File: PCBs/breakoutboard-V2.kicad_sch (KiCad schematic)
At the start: 38 parts, among them IC1 PASCO2V01BUMA1, J1 Conn_01x12_FPC_0.5mm, J2 Qwiic_RA, J4 SM06B-GHS-TB, J5 USB_C_Receptacle, SW1 SMD_4.6x2.8mm_h2.5mm, SW2 SMD_4.6x2.8mm_h2.5mm, SW3 PTH_RA_h7.5mm, U1 AP3012, U2 ESP32-S3-WROOM-1-N16R2, U5 AP2112K-3.3

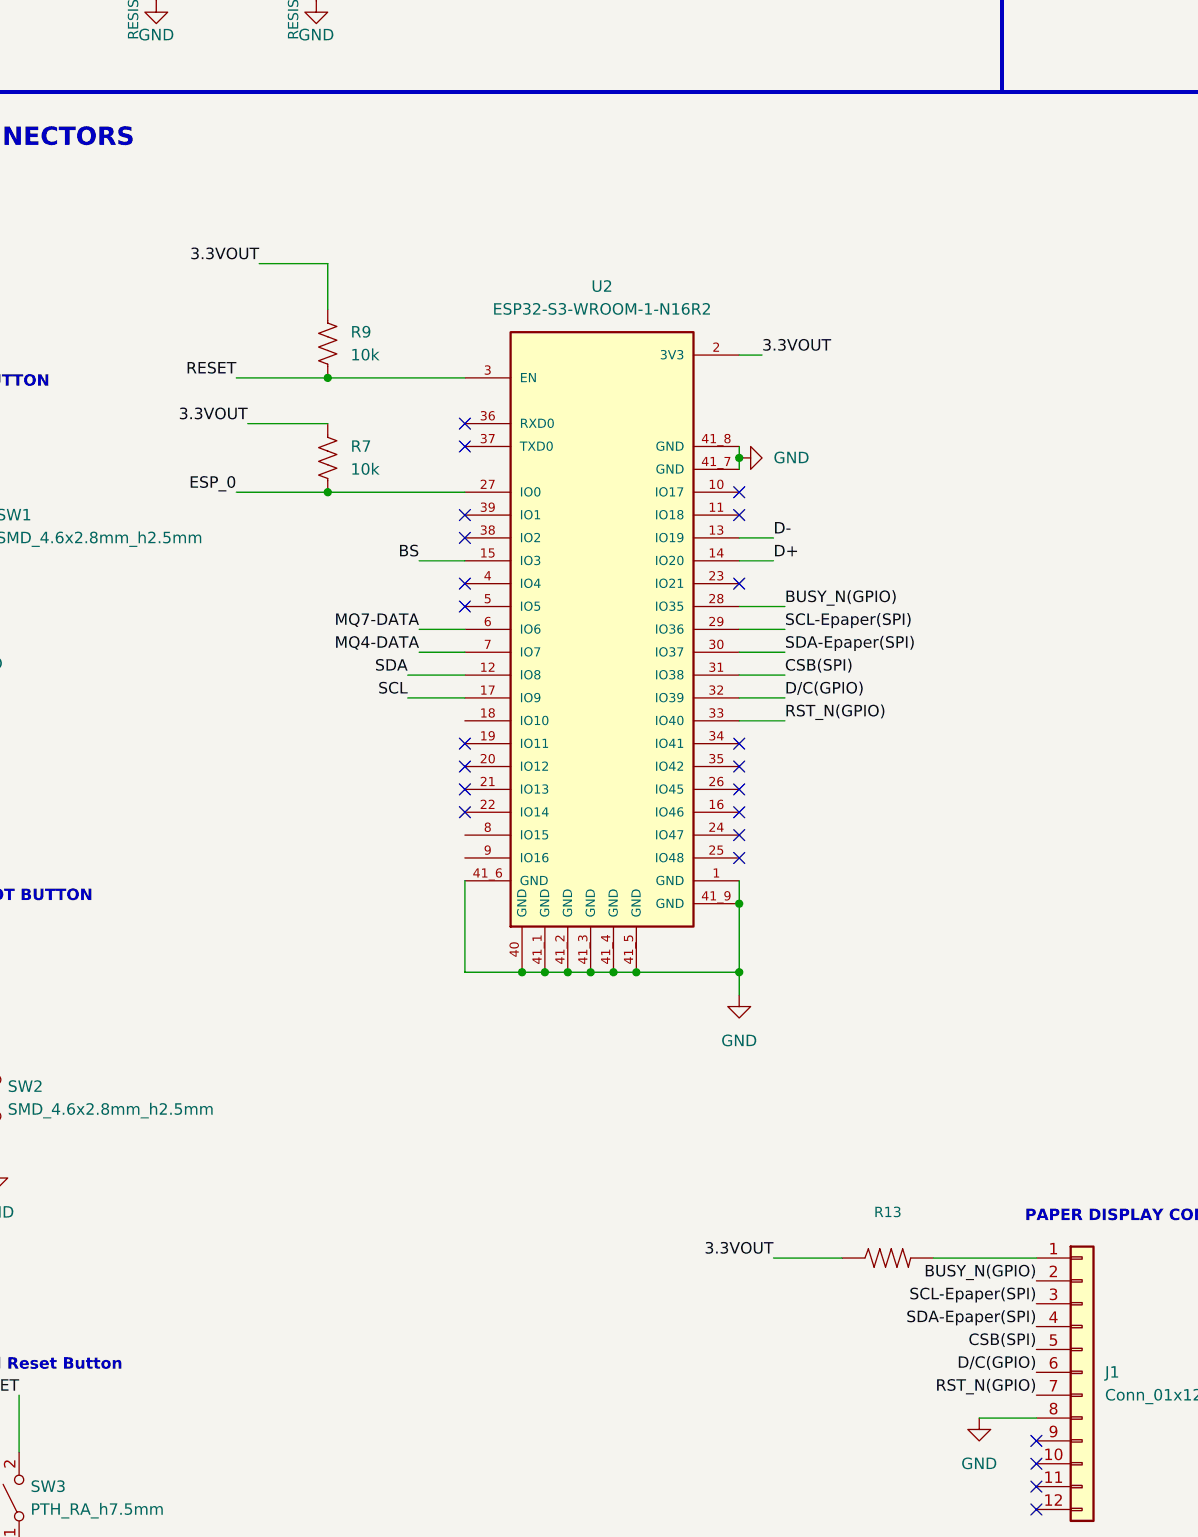
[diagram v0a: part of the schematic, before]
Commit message: Update Main Board PCB
Replaced ESP32 WROOM with ESP32 mini. READY FOR AIR WIRE REVIEW :D
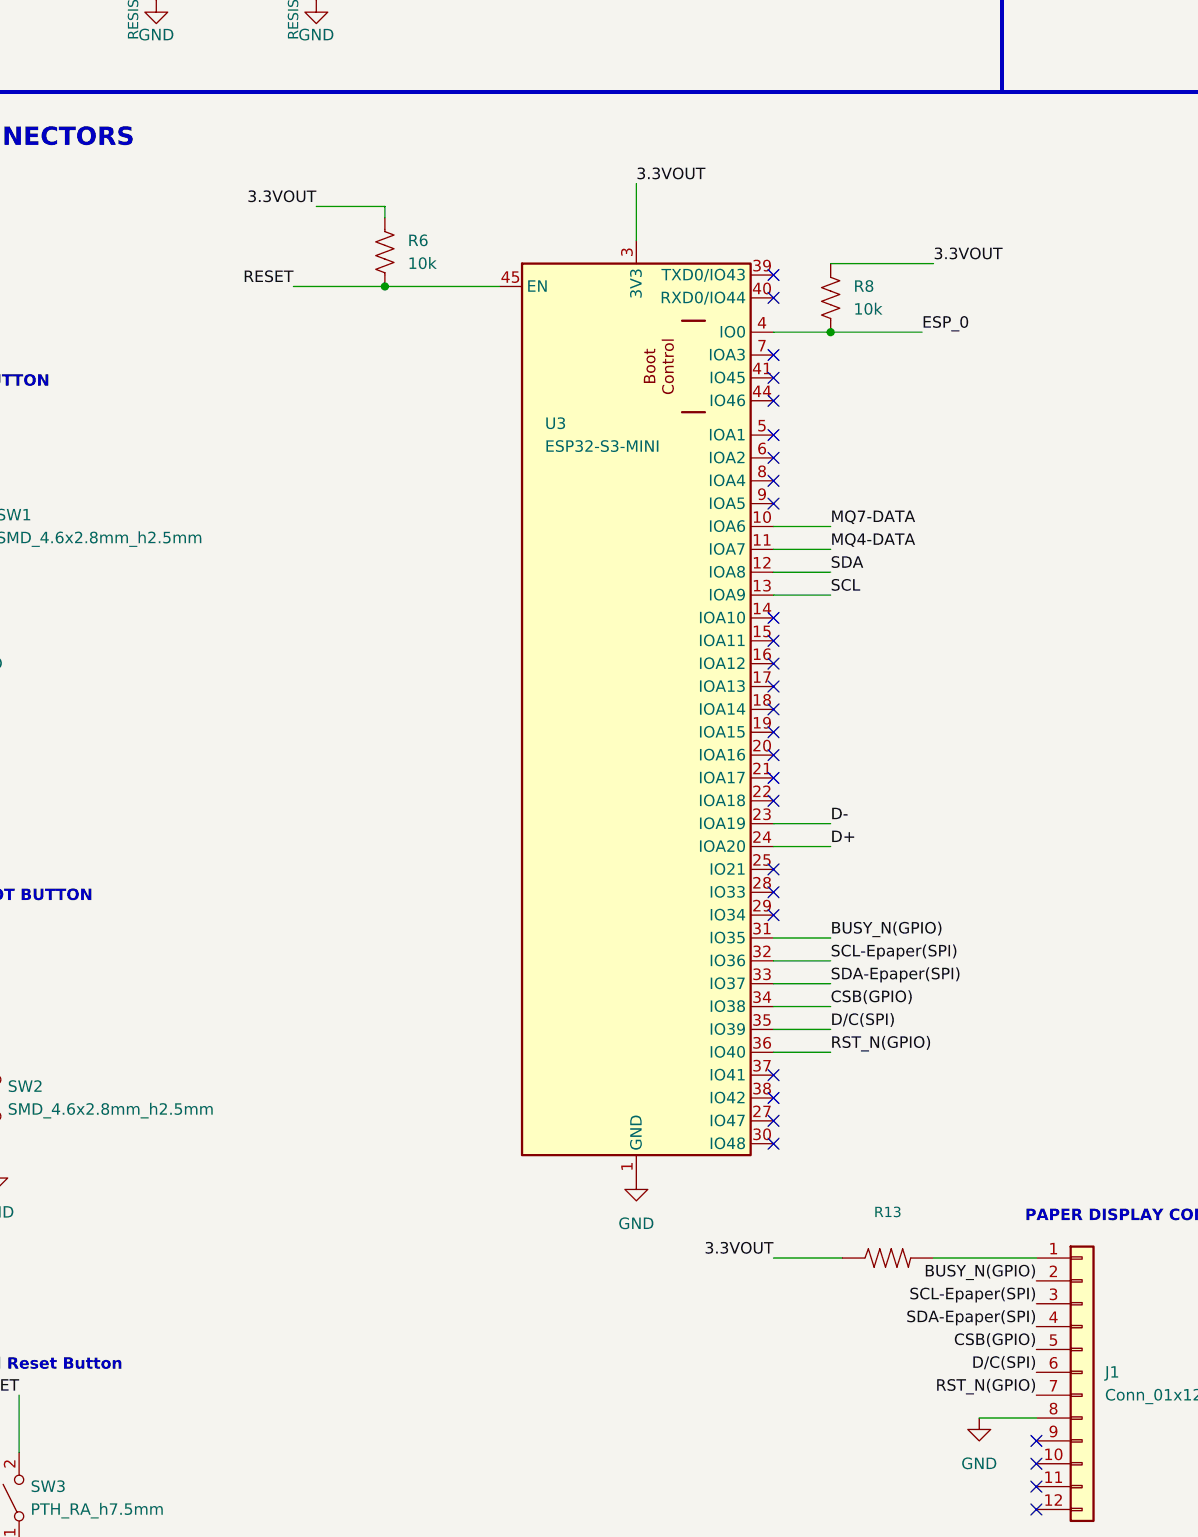
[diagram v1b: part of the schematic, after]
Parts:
- removed R7, R9: 10k, SparkFun-Resistor:R_0402_1005Metric, symbol SparkFun-Resistor:10k_0402
- removed U2: ESP32-S3-WROOM-1-N16R2, ESP32-S3-WROOM-1-N16R2:XCVR_ESP32-S3-WROOM-1-N16R2, symbol ESP32-S3-WROOM-1-N16R2:ESP32-S3-WROOM-1-N16R2
- added R6, R8: 10k, SparkFun-Resistor:R_0402_1005Metric, symbol SparkFun-Resistor:10k_0402
- added U3: ESP32-S3-MINI, SparkFun-RF:ESP32-MINI, symbol SparkFun-RF:ESP32-S3-MINI
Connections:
- net 3.3VOUT: now also R6.1, R8.1, U3.3 (3V3)
- net BUSY_N(GPIO): now also U3.31 (IO35)
- net D+: now also U3.24 (IOA20)
- net D-: now also U3.23 (IOA19)
- net ESP_0: now also R8.2, U3.4 (IO0)
- net GND: now also U3.1 (GND), U3.2 (GND), U3.42 (GND), U3.43 (GND), U3.46 (GND), U3.47 (GND), U3.48 (GND), U3.49 (GND), U3.50 (GND), U3.51 (GND), U3.52 (GND), U3.53 (GND), U3.54 (GND), U3.55 (GND), U3.56 (GND), U3.57 (GND), U3.58 (GND), U3.59 (GND), U3.60 (GND), U3.61 (GND), U3.62 (GND), U3.63 (GND), U3.64 (GND), U3.65 (GND)
- net MQ4-DATA: now also U3.11 (IOA7)
- net MQ7-DATA: now also U3.10 (IOA6)
- net RESET: now also R6.2, U3.45 (EN)
- net RST_N(GPIO): now also U3.36 (IO40)
- net SCL: now also U3.13 (IOA9)
- net SCL-Epaper(SPI): now also U3.32 (IO36)
- net SDA: now also U3.12 (IOA8)
- net SDA-Epaper(SPI): now also U3.33 (IO37)
- net CSB(SPI) renamed CSB(GPIO)
- net CSB(GPIO): now also U3.34 (IO38)
- net D/C(GPIO) renamed D/C(SPI)
- net D/C(SPI): now also U3.35 (IO39)
- no-connect marks 32 -> 38
